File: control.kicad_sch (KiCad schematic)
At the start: 49 parts, among them J101 Cortex_Debug, J102 JAE_DX07S016JA3, J103 WAGO-2065, J104 WAGO-2065, SW101 SW_Push, SW102 SW_Push, U101 TPS78433QWDRBRQ1, U102 ATSAMD51G, Y101 32k768

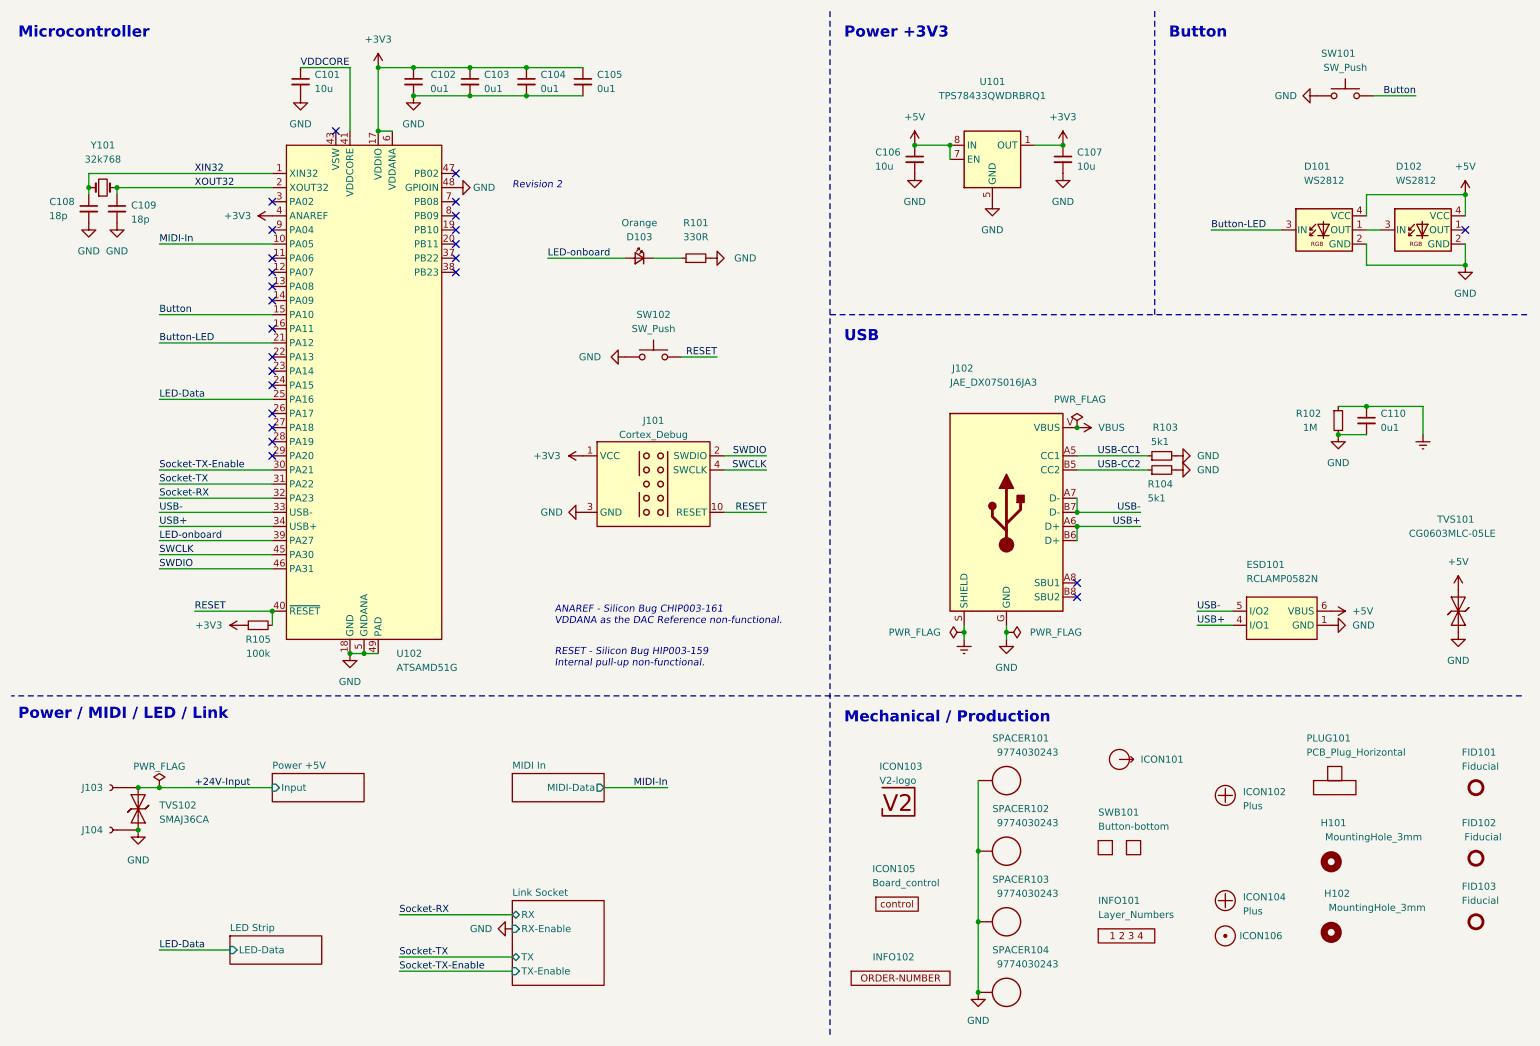
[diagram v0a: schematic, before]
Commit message: Replace Order_Number
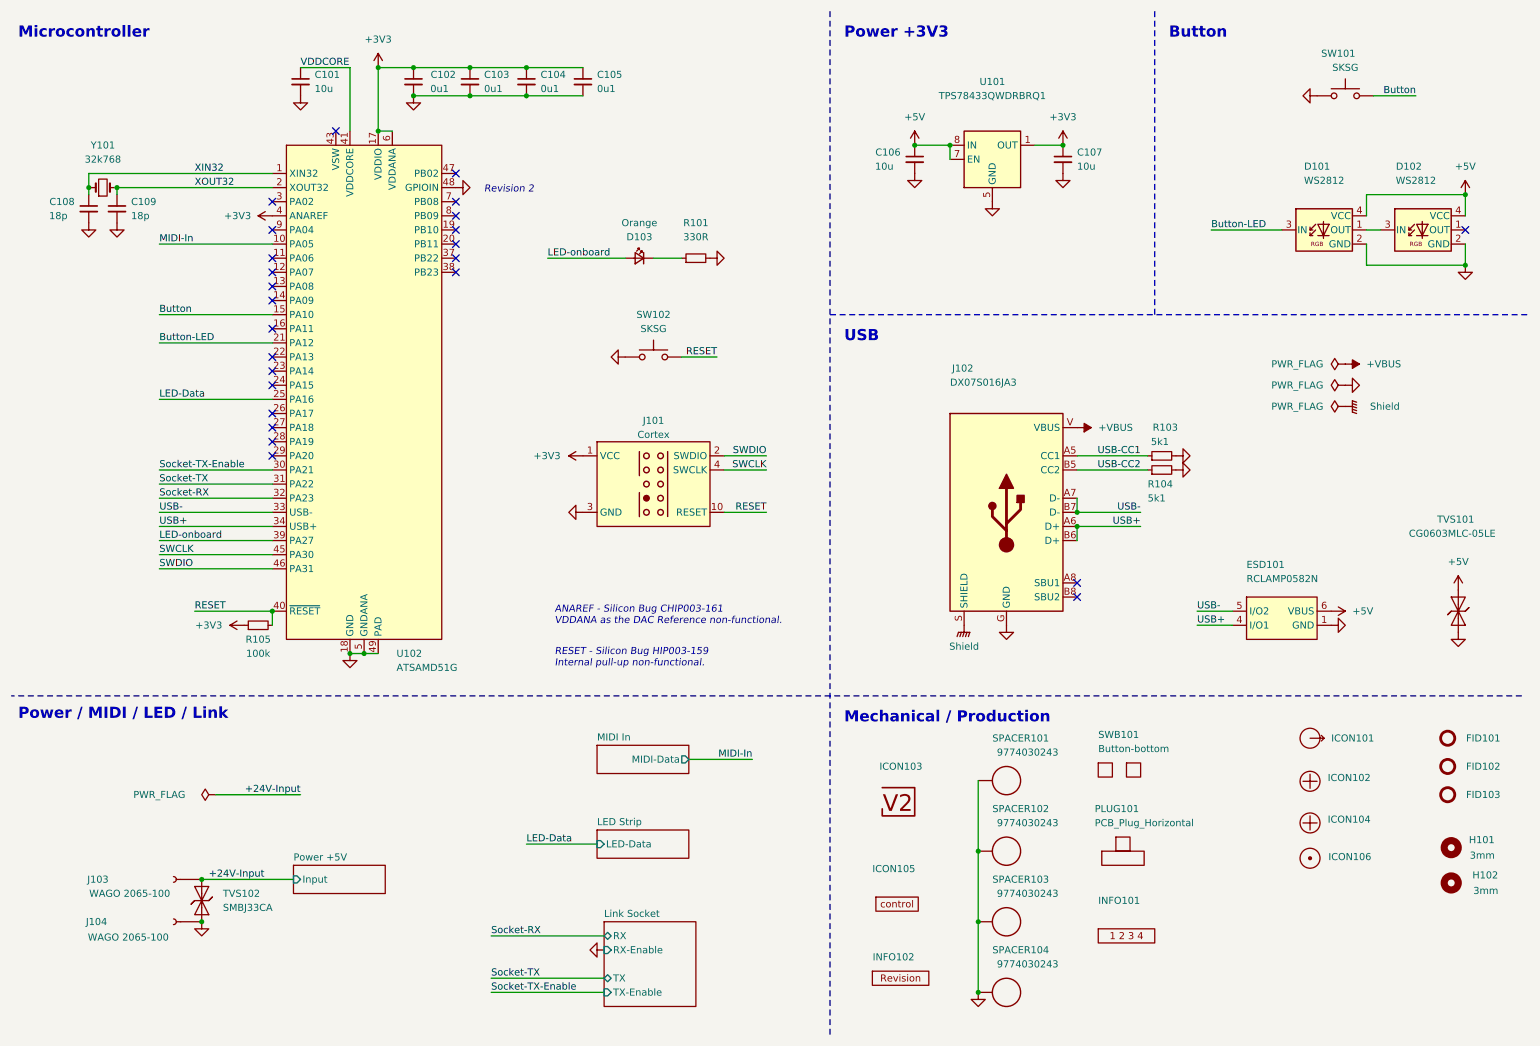
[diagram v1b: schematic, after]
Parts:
- removed C110: 0u1, Capacitor_SMD:C_0603_1608Metric, symbol Device:C_Small
- removed R102: 1M, Resistor_SMD:R_0603_1608Metric, symbol Device:R_Small
- C101: footprint Capacitor_SMD:C_0603_1608Metric -> V2_Capacitor_SMD:C_0603; symbol Device:C_Small -> V2_Device:C_0603_10u; Manufacturer (none) -> TDK; Mouser (none) -> 810-C1608X6S1A106M; Product (none) -> C1608X6S1A106M080AC; Rating (none) -> 10V
- C102, C103, C104, C105: footprint Capacitor_SMD:C_0603_1608Metric -> V2_Capacitor_SMD:C_0603; symbol Device:C_Small -> V2_Device:C_0603_0u1; Manufacturer (none) -> TDK; Mouser (none) -> 810-CGA3E2X7R1H104MA; Product (none) -> CGA3E2X7R1H104M080AA; Rating (none) -> 50V
- C106, C107: footprint Capacitor_SMD:C_0603_1608Metric -> V2_Capacitor_SMD:C_0805; symbol Device:C_Small -> V2_Device:C_0805_10u; Manufacturer (none) -> TDK; Mouser (none) -> 810-C2012X5R1E106K; Product (none) -> C2012X5R1E106K125AB; Rating (none) -> 25V
- C108, C109: footprint Capacitor_SMD:C_0603_1608Metric -> V2_Capacitor_SMD:C_0603; symbol Device:C_Small -> V2_Device:C_0603_18p; Manufacturer (none) -> YAGEO; Mouser (none) -> 603-CC603JRNPO9BN180; Product (none) -> CC0603JRNPO9BN180
- D101, D102: LCSC (none) -> C965555; Manufacturer (none) -> Worldsemi; Product (none) -> WS2812B-2020
- D103: footprint LED_SMD:LED_0603_1608Metric -> V2_LED:LED_0603; symbol Device:LED_Small -> V2_Device:LED_0603_Orange; Manufacturer (none) -> ROHM Semiconductor; Mouser (none) -> 755-SML-D12D1WT86; Product (none) -> SML-D12D1WT86
- ESD101: Manufacturer (none) -> Semtech; Mouser (none) -> 947-RCLAMP0582N.TCT; Product (none) -> RCLAMP0582N.TCT
- FID101, FID102, FID103: value Fiducial -> Fiducial_Paste
- H101, H102: value MountingHole_3mm -> 3mm
- INFO102: value ORDER-NUMBER -> (none); footprint V2_Production:Order_Number -> V2_Production:Revision; symbol V2_Production:Order_Number -> V2_Production:Revision
- J101: value Cortex_Debug -> Cortex; footprint V2_Cortex_Debug:Cortex_Debug_Pad -> V2_Connector_Debug:Cortex; symbol V2_Cortex_Debug:Cortex_Debug -> V2_Connector_Debug:Cortex
- J102: value JAE_DX07S016JA3 -> DX07S016JA3; Manufacturer (none) -> JAE Electronics; Mouser (none) -> 656-DX07S016JA3R1500; Product (none) -> DX07S016JA3R1500
- J103, J104: value WAGO-2065 -> WAGO 2065-100; Manufacturer (none) -> WAGO; Product (none) -> 2065-100/998-403
- R101: footprint Resistor_SMD:R_0603_1608Metric -> V2_Resistor_SMD:R_0603; symbol Device:R_Small -> V2_Device:R_0603_330R; Manufacturer (none) -> Vishay; Mouser (none) -> 71-CRCW0603330RFKEAC; Product (none) -> CRCW0603330RFKEAC; Rating (none) -> 100mW
- R103, R104: footprint Resistor_SMD:R_0603_1608Metric -> V2_Resistor_SMD:R_0603; symbol Device:R_Small -> V2_Device:R_0603_5k1; Manufacturer (none) -> Vishay; Mouser (none) -> 71-CRCW06035K10FKEAC; Product (none) -> CRCW06035K10FKEAC; Rating (none) -> 100mW
- R105: footprint Resistor_SMD:R_0603_1608Metric -> V2_Resistor_SMD:R_0603; symbol Device:R_Small -> V2_Device:R_0603_100k; Manufacturer (none) -> Vishay; Mouser (none) -> 71-CRCW0603100KFKEAC; Product (none) -> CRCW0603100KFKEAC; Rating (none) -> 100mW
- SW101, SW102: value SW_Push -> SKSG; symbol Switch:SW_Push -> V2_Switch:SKSG; Manufacturer (none) -> Alps Alpine; Mouser (none) -> 688-SKSGACE010; Product (none) -> SKSGACE010
- TVS101: footprint Diode_SMD:D_0603_1608Metric -> V2_Diode_SMD:D_0603; Manufacturer (none) -> Bourns; Mouser (none) -> 652-CG0603MLC-05LE; Product (none) -> CG0603MLC-05LE; Rating (none) -> 5V
- TVS102: value SMAJ36CA -> SMBJ33CA; footprint Diode_SMD:D_SMA -> V2_Diode_SMD:D_SMB; symbol V2_Diode:SMAJ36CA -> V2_Diode:SMBJ33CA; Manufacturer (none) -> Bourns; Mouser (none) -> 652-SMBJ33CA-Q; Product (none) -> SMBJ33CA-Q; Rating (none) -> 33V
- U101: Manufacturer (none) -> Texas Instruments; Mouser (none) -> 595-TPS78433QWDRBRQ1; Product (none) -> TPS78433QWDRBRQ1
- U102: Manufacturer (none) -> Microchip Technology; Mouser (none) -> 556-ATSAMD51G19AMU; Product (none) -> ATSAMD51G19A-MU
- Y101: symbol Device:Crystal_Small -> V2_Device:Crystal_3.2x1.5_32k768; Manufacturer (none) -> ABRACON; Mouser (none) -> 815-ABS0716632.768KT; Product (none) -> ABS07-166-32.768KHZ-T
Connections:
- net Earth renamed Shield
- net VBUS renamed +VBUS
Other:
- moved on the sheet: FID101, FID102, FID103, H101, H102, ICON101, ICON102, ICON104, ICON106, J103, J104, PLUG101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

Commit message: Update Library
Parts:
- C101: symbol V2_Device:C_0603_10u -> V2_Capacitor:0603_10u
- C102, C103, C104, C105: symbol V2_Device:C_0603_0u1 -> V2_Capacitor:0603_0u1
- C106, C107: symbol V2_Device:C_0805_10u -> V2_Capacitor:0805_10u
- C108, C109: symbol V2_Device:C_0603_18p -> V2_Capacitor:0603_18p
- D103: symbol V2_Device:LED_0603_Orange -> V2_LED:0603_Orange
- INFO102: value (none) -> ~
- R101: symbol V2_Device:R_0603_330R -> V2_Resistor:0603_330R
- R103, R104: symbol V2_Device:R_0603_5k1 -> V2_Resistor:0603_5k1
- R105: symbol V2_Device:R_0603_100k -> V2_Resistor:0603_100k
- Y101: symbol V2_Device:Crystal_3.2x1.5_32k768 -> V2_Crystal:3.2x1.5_32k768

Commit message: Refresh
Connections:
- net +24V-Input renamed +28V
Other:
- moved on the sheet: J103, J104, TVS102

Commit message: Update ESD suppressor
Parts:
- C108, C109: Manufacturer YAGEO -> TDK; Mouser 603-CC603JRNPO9BN180 -> 810-CGA3E2C0G1H180J; Product CC0603JRNPO9BN180 -> CGA3E2C0G1H180J080AA
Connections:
- no-connect marks 25 -> 27
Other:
- moved on the sheet: J102, R103, R104, TVS101

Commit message: Replace diode
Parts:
- INFO102: value ~ -> (none)

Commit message: Replace step-down
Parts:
- C108, C109: Rating (none) -> 50V
- SW101, SW102: Rating (none) -> 1.6N
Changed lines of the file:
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@@
 			)
 		)
+		(property "Rating" "1.6N"
+			(at 252.73 48.26 0)
+			(hide yes)
+			(show_name no)
+			(do_not_autoplace no)
+			(effects
+				(font
+					(size 1.27 1.27)
+				)
+			)
+		)
 		(pin "1"
 		)
@@
 			)
 		)
+		(property "Sim.Enable" "0"
+			(at 212.09 149.225 0)
+			(hide yes)
+			(show_name no)
+			(do_not_autoplace no)
+			(effects
+				(font
+					(size 1.27 1.27)
+				)
+			)
+		)
 		(instances
 			(project "control"
@@
 			)
 		)
+		(property "Sim.Enable" "0"
+			(at 212.725 163.83 0)
+			(hide yes)
+			(show_name no)
+			(do_not_autoplace no)
+			(effects
+				(font
+					(size 1.27 1.27)
+				)
+			)
+		)
 		(instances
 			(project "control"
@@
 			)
 		)
+		(property "Sim.Enable" "0"
+			(at 246.38 143.51 0)
+			(hide yes)
+			(show_name no)
+			(do_not_autoplace no)
+			(effects
+				(font
+					(size 1.27 1.27)
+				)
+			)
+		)
 		(instances
 			(project "control"
@@
 			)
 		)
+		(property "Sim.Enable" "0"
+			(at 172.085 173.355 0)
+			(hide yes)
+			(show_name no)
+			(do_not_autoplace no)
+			(effects
+				(font
+					(size 1.27 1.27)
+				)
+			)
+		)
 		(instances
 			(project "control"
@@
 			)
 		)
+		(property "Sim.Enable" "0"
+			(at 246.38 158.75 0)
+			(hide yes)
+			(show_name no)
+			(do_not_autoplace no)
+			(effects
+				(font
+					(size 1.27 1.27)
+				)
+			)
+		)
 		(instances
 			(project "control"
@@
 			)
 		)
+		(property "Rating" "50V"
+			(at 31.75 73.66 0)
+			(hide yes)
+			(show_name no)
+			(do_not_autoplace no)
+			(effects
+				(font
+					(size 1.27 1.27)
+				)
+			)
+		)
 		(pin "1"
 		)
@@
 			)
 		)
+		(property "Rating" "50V"
+			(at 26.67 73.66 0)
+			(hide yes)
+			(show_name no)
+			(do_not_autoplace no)
+			(effects
+				(font
+					(size 1.27 1.27)
+				)
+			)
+		)
 		(pin "1"
 		)
@@
 			)
 		)
+		(property "Rating" "1.6N"
+			(at 128.27 95.25 0)
+			(hide yes)
+			(show_name no)
+			(do_not_autoplace no)
+			(effects
+				(font
+					(size 1.27 1.27)
+				)
+			)
+		)
 		(pin "1"
 		)
@@
 			)
 		)
+		(property "Sim.Enable" "0"
+			(at 246.38 165.1 0)
+			(hide yes)
+			(show_name no)
+			(do_not_autoplace no)
+			(effects
+				(font
+					(size 1.27 1.27)
+				)
+			)
+		)
 		(instances
 			(project "control"
@@
 			(at 246.38 151.257 0)
 			(hide yes)
+			(show_name no)
+			(do_not_autoplace no)
+			(effects
+				(font
+					(size 1.27 1.27)
+				)
+			)
+		)
+		(property "Sim.Enable" "0"
+			(at 246.38 151.257 0)
+			(hide yes)

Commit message: Good Bye Imperial
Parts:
- C101: footprint V2_Capacitor_SMD:C_0603 -> V2_Capacitor_SMD:C_1608; symbol V2_Capacitor:0603_10u -> V2_Capacitor:1608_10u
- C102, C103, C104, C105: footprint V2_Capacitor_SMD:C_0603 -> V2_Capacitor_SMD:C_1608; symbol V2_Capacitor:0603_0u1 -> V2_Capacitor:1608_0u1
- C106, C107: footprint V2_Capacitor_SMD:C_0805 -> V2_Capacitor_SMD:C_2012; symbol V2_Capacitor:0805_10u -> V2_Capacitor:2012_10u
- C108, C109: footprint V2_Capacitor_SMD:C_0603 -> V2_Capacitor_SMD:C_1608; symbol V2_Capacitor:0603_18p -> V2_Capacitor:1608_18p
- D103: symbol V2_LED:0603_Orange -> V2_LED:1608_Orange
- R101: footprint V2_Resistor_SMD:R_0603 -> V2_Resistor_SMD:R_1608; symbol V2_Resistor:0603_330R -> V2_Resistor:1608_330R
- R103, R104: footprint V2_Resistor_SMD:R_0603 -> V2_Resistor_SMD:R_1608; symbol V2_Resistor:0603_5k1 -> V2_Resistor:1608_5k1
- R105: footprint V2_Resistor_SMD:R_0603 -> V2_Resistor_SMD:R_1608; symbol V2_Resistor:0603_100k -> V2_Resistor:1608_100k
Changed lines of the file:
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@@
 	)
 	(symbol
-		(lib_id "V2_Capacitor:0603_0u1")
+		(lib_id "V2_Capacitor:1608_0u1")
 		(at 115.57 25.4 0)
 		(unit 1)
@@
 			)
 		)
-		(property "Footprint" "V2_Capacitor_SMD:C_0603"
+		(property "Footprint" "V2_Capacitor_SMD:C_1608"
 			(at 115.57 42.418 0)
 			(hide yes)
@@
 	)
 	(symbol
-		(lib_id "V2_LED:0603_Orange")
+		(lib_id "V2_LED:1608_Orange")
 		(at 125.73 57.15 0)
 		(mirror y)
@@
 	)
 	(symbol
-		(lib_id "V2_Capacitor:0805_10u")
+		(lib_id "V2_Capacitor:2012_10u")
 		(at 201.93 39.37 0)
 		(unit 1)
@@
 			)
 		)
-		(property "Footprint" "V2_Capacitor_SMD:C_0805"
+		(property "Footprint" "V2_Capacitor_SMD:C_2012"
 			(at 201.93 56.388 0)
 			(hide yes)
@@
 	)
 	(symbol
-		(lib_id "V2_Resistor:0603_5k1")
+		(lib_id "V2_Resistor:1608_5k1")
 		(at 215.9 96.52 90)
 		(unit 1)
@@
 			)
 		)
-		(property "Footprint" "V2_Resistor_SMD:R_0603"
+		(property "Footprint" "V2_Resistor_SMD:R_1608"
 			(at 231.648 96.52 0)
 			(hide yes)
@@
 	)
 	(symbol
-		(lib_id "V2_Capacitor:0805_10u")
+		(lib_id "V2_Capacitor:2012_10u")
 		(at 175.26 39.37 0)
 		(unit 1)
@@
 			)
 		)
-		(property "Footprint" "V2_Capacitor_SMD:C_0805"
+		(property "Footprint" "V2_Capacitor_SMD:C_2012"
 			(at 175.26 56.388 0)
 			(hide yes)
@@
 	)
 	(symbol
-		(lib_id "V2_Capacitor:0603_18p")
+		(lib_id "V2_Capacitor:1608_18p")
 		(at 31.75 48.26 0)
 		(unit 1)
@@
 			)
 		)
-		(property "Footprint" "V2_Capacitor_SMD:C_0603"
+		(property "Footprint" "V2_Capacitor_SMD:C_1608"
 			(at 31.75 65.278 0)
 			(hide yes)
@@
 	)
 	(symbol
-		(lib_id "V2_Capacitor:0603_10u")
+		(lib_id "V2_Capacitor:1608_10u")
 		(at 64.77 25.4 0)
 		(unit 1)
@@
 			)
 		)
-		(property "Footprint" "V2_Capacitor_SMD:C_0603"
+		(property "Footprint" "V2_Capacitor_SMD:C_1608"
 			(at 64.77 42.418 0)
 			(hide yes)
@@
 	)
 	(symbol
-		(lib_id "V2_Capacitor:0603_18p")
+		(lib_id "V2_Capacitor:1608_18p")
 		(at 26.67 48.26 0)
 		(unit 1)
@@
 			)
 		)
-		(property "Footprint" "V2_Capacitor_SMD:C_0603"
+		(property "Footprint" "V2_Capacitor_SMD:C_1608"
 			(at 26.67 65.278 0)
 			(hide yes)
@@
 	)
 	(symbol
-		(lib_id "V2_Resistor:0603_330R")
+		(lib_id "V2_Resistor:1608_330R")
 		(at 135.89 57.15 90)
 		(unit 1)
@@
 			)
 		)
-		(property "Footprint" "V2_Resistor_SMD:R_0603"
+		(property "Footprint" "V2_Resistor_SMD:R_1608"
 			(at 151.638 57.15 0)
 			(hide yes)
@@
 	)
 	(symbol
-		(lib_id "V2_Capacitor:0603_0u1")
+		(lib_id "V2_Capacitor:1608_0u1")
 		(at 105.41 25.4 0)
 		(unit 1)
@@
 			)
 		)
-		(property "Footprint" "V2_Capacitor_SMD:C_0603"
+		(property "Footprint" "V2_Capacitor_SMD:C_1608"
 			(at 105.41 42.418 0)
 			(hide yes)
@@
 	)
 	(symbol
-		(lib_id "V2_Capacitor:0603_0u1")
+		(lib_id "V2_Capacitor:1608_0u1")
 		(at 85.09 25.4 0)
 		(unit 1)
@@
 			)
 		)
-		(property "Footprint" "V2_Capacitor_SMD:C_0603"
+		(property "Footprint" "V2_Capacitor_SMD:C_1608"
 			(at 85.09 42.418 0)
 			(hide yes)
@@
 	)
 	(symbol
-		(lib_id "V2_Capacitor:0603_0u1")
+		(lib_id "V2_Capacitor:1608_0u1")
 		(at 95.25 25.4 0)
 		(unit 1)
@@
 			)
 		)
-		(property "Footprint" "V2_Capacitor_SMD:C_0603"
+		(property "Footprint" "V2_Capacitor_SMD:C_1608"
 			(at 95.25 42.418 0)
 			(hide yes)
@@
 	)
 	(symbol
-		(lib_id "V2_Resistor:0603_5k1")
+		(lib_id "V2_Resistor:1608_5k1")
 		(at 215.9 93.98 90)
 		(unit 1)
@@
 			)
 		)
-		(property "Footprint" "V2_Resistor_SMD:R_0603"
+		(property "Footprint" "V2_Resistor_SMD:R_1608"
 			(at 231.648 93.98 0)
 			(hide yes)
@@
 	)
 	(symbol
-		(lib_id "V2_Resistor:0603_100k")
+		(lib_id "V2_Resistor:1608_100k")
 		(at 57.15 123.19 90)
 		(unit 1)
@@
 			)
 		)
-		(property "Footprint" "V2_Resistor_SMD:R_0603"
+		(property "Footprint" "V2_Resistor_SMD:R_1608"
 			(at 72.898 123.19 0)
 			(hide yes)
